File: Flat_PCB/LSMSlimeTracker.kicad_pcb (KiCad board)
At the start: 2 copper layers, 40 x 30.5 mm, 49 parts, among them J1 USB_C_Receptacle_USB2.0, J2 Conn_01x04_Socket, Q1 Q_PMOS_GSD, SW1 SW_Push, SW2 SW_SPDT, SW3 SW_Push, U1 LSM6DSV16X, U2 M3406, U3 ESP32-C3-WROOM-02-N4, U7 BQ24040DSQT

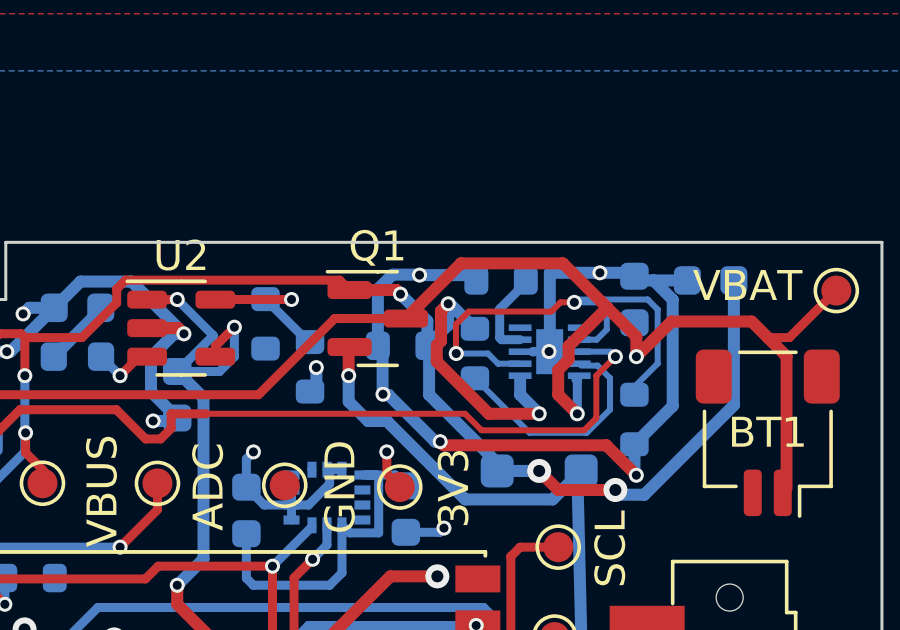
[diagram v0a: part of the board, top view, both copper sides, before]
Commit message: TTDM fix
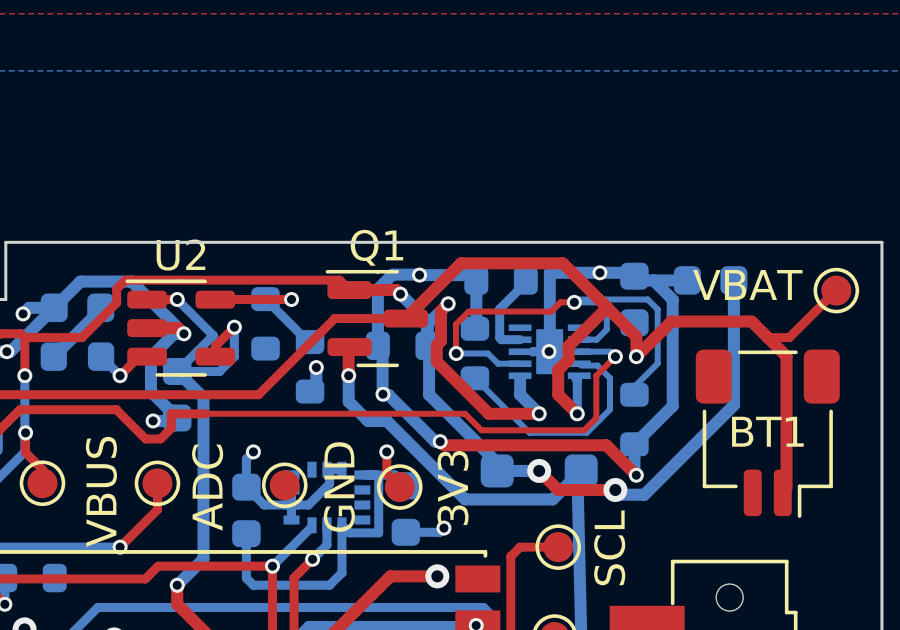
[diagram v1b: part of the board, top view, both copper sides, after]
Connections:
- R8 pad 2: +5V -> GND
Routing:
- net GND: track 72.7 -> 74.3 mm
- net +5V: track 61.3 -> 59.9 mm
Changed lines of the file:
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@@
       )
     )
-    (model "/Projects/kicad-custom-models/ESP32-C3-WROOM-02-N4.step"
+    (model "${KIPRJMOD}/custom-models/ESP32-C3-WROOM-02-N4.step"
       (offset (xyz 0 0 0))
       (scale (xyz 1 1 1))
@@
       (net 37 "/TS") (pintype "passive"))
     (pad "2" smd roundrect (at 0.825 0 90) (size 0.8 0.95) (layers "B.Cu" "B.Paste" "B.Mask") (roundrect_rratio 0.25)
-      (net 3 "+5V") (pintype "passive"))
+      (net 1 "GND") (pintype "passive"))
     (model "${KICAD6_3DMODEL_DIR}/Resistor_SMD.3dshapes/R_0603_1608Metric.wrl"
       (offset (xyz 0 0 0))
@@
     (pad "11" smd rect (at 0 0) (size 0.9 1.5) (layers "B.Cu" "B.Mask")
       (net 1 "GND") (pinfunction "EP") (pintype "bidirectional"))
-    (model "/Projects/kicad-custom-models/BQ24040DSQT.step"
+    (model "${KIPRJMOD}/custom-models/BQ24040DSQT.step"
       (offset (xyz 0 0 0))
       (scale (xyz 1 1 1))
@@
   (segment (start 182.88 54.567963) (end 183.291226 54.567963) (width 0.3) (layer "B.Cu") (net 1))
   (segment (start 171.572343 52.705) (end 171.572343 53.623467) (width 0.4) (layer "B.Cu") (net 1))
+  (segment (start 187.77 49.825077) (end 187.724238 49.870839) (width 0.4) (layer "B.Cu") (net 1))
   (segment (start 184.836117 52.07) (end 186.399927 53.63381) (width 0.4) (layer "B.Cu") (net 1))
   (segment (start 177.701164 52.943836) (end 177.8 52.845) (width 0.4) (layer "B.Cu") (net 1))
@@
   (segment (start 190.22 50.603401) (end 190.193419 50.629982) (width 0.4) (layer "B.Cu") (net 1))
   (segment (start 186.019256 65.477202) (end 186.055 65.512946) (width 0.4) (layer "B.Cu") (net 1))
+  (segment (start 187.77 48.26) (end 187.77 49.825077) (width 0.4) (layer "B.Cu") (net 1))
   (segment (start 182.88 55.041826) (end 182.88 54.567963) (width 0.3) (layer "B.Cu") (net 1))
   (segment (start 177.73975 70.19025) (end 177.8 70.13) (width 0.4) (layer "B.Cu") (net 1))
@@
   (segment (start 169.980041 49.809642) (end 168.187858 49.809642) (width 0.3) (layer "B.Cu") (net 3))
   (segment (start 189.865 52.705) (end 189.23 52.07) (width 0.4) (layer "B.Cu") (net 3))
+  (segment (start 186.138168 49.730364) (end 186.831766 49.036766) (width 0.4) (layer "B.Cu") (net 3))
   (segment (start 193.372025 55.403358) (end 192.563358 55.403358) (width 0.4) (layer "B.Cu") (net 3))
   (segment (start 172.72 53.975) (end 171.45 55.245) (width 0.3) (layer "B.Cu") (net 3))
@@
   (segment (start 188.465 54.61) (end 188.465 54.34) (width 0.4) (layer "B.Cu") (net 3))
   (segment (start 189.23 52.07) (end 189.23 51.535) (width 0.4) (layer "B.Cu") (net 3))
-  (segment (start 186.831766 49.036766) (end 186.831766 49.745647) (width 0.4) (layer "B.Cu") (net 3))
   (segment (start 186.195 52.07) (end 186.195 50.496077) (width 0.4) (layer "B.Cu") (net 3))
-  (segment (start 186.831766 49.745647) (end 186.013773 50.56364) (width 0.4) (layer "B.Cu") (net 3))
   (segment (start 186.138168 49.613167) (end 186.138168 50.439245) (width 0.4) (layer "B.Cu") (net 3))
   (segment (start 196.355 48.26) (end 196.355 52.420383) (width 0.4) (layer "B.Cu") (net 3))
+  (segment (start 186.138168 50.439245) (end 186.138168 49.730364) (width 0.4) (layer "B.Cu") (net 3))
   (segment (start 196.355 52.420383) (end 193.372025 55.403358) (width 0.4) (layer "B.Cu") (net 3))
   (segment (start 172.744541 53.341365) (end 172.72 53.365906) (width 0.3) (layer "B.Cu") (net 3))
@@
   (segment (start 185.242181 48.71718) (end 186.138168 49.613167) (width 0.4) (layer "B.Cu") (net 3))
   (segment (start 170.261049 50.09065) (end 169.980041 49.809642) (width 0.3) (layer "B.Cu") (net 3))
-  (segment (start 186.890165 49.036766) (end 187.724238 49.870839) (width 0.4) (layer "B.Cu") (net 3))
   (segment (start 170.343404 50.09065) (end 170.261049 50.09065) (width 0.3) (layer "B.Cu") (net 3))
   (segment (start 186.195 50.496077) (end 186.138168 50.439245) (width 0.4) (layer "B.Cu") (net 3))
@@
   (segment (start 168.857466 54.62) (end 167.9775 54.62) (width 0.3) (layer "B.Cu") (net 3))
   (segment (start 188.465 54.34) (end 186.195 52.07) (width 0.4) (layer "B.Cu") (net 3))
-  (segment (start 186.831766 49.036766) (end 186.890165 49.036766) (width 0.4) (layer "B.Cu") (net 3))
   (segment (start 162.56 49.53) (end 165.1 49.53) (width 0.3) (layer "F.Cu") (net 4))
   (segment (start 169.935717 53.636841) (end 169.893876 53.595) (width 0.3) (layer "B.Cu") (net 5))

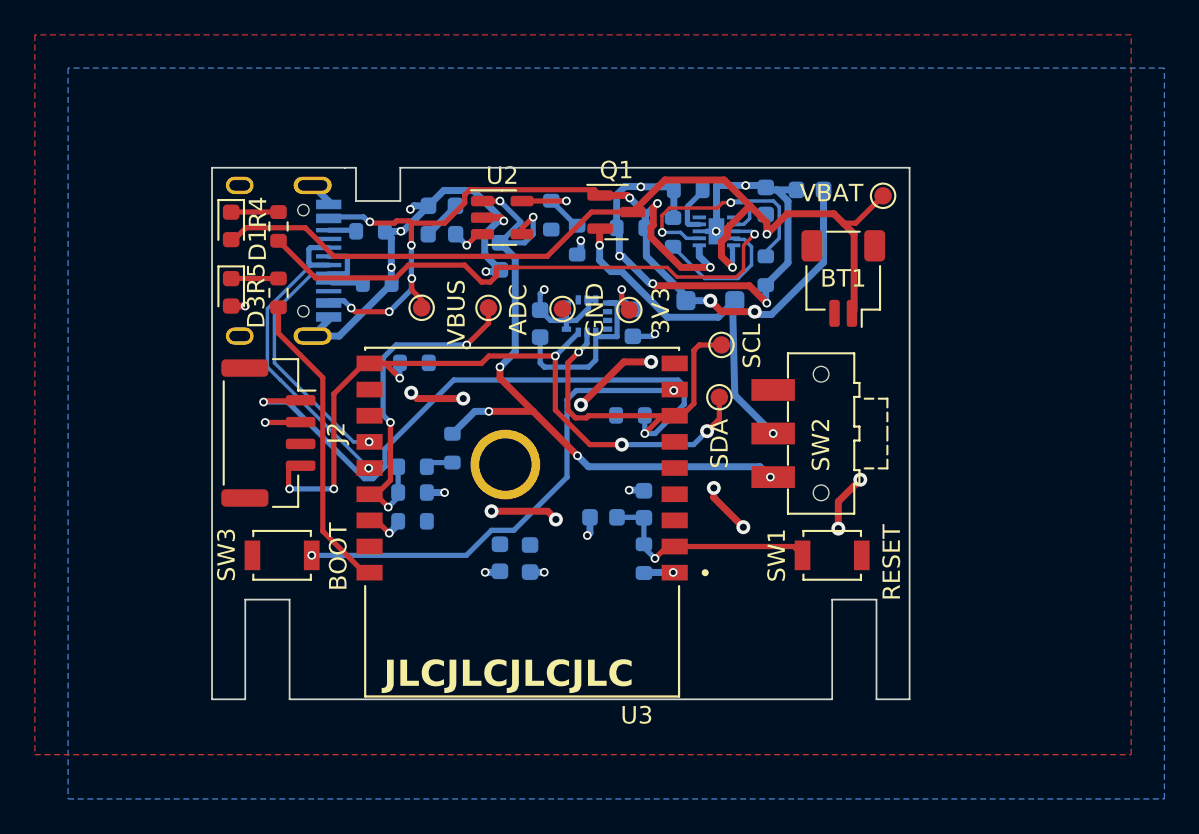
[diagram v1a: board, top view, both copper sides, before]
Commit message: Moved USB C to top
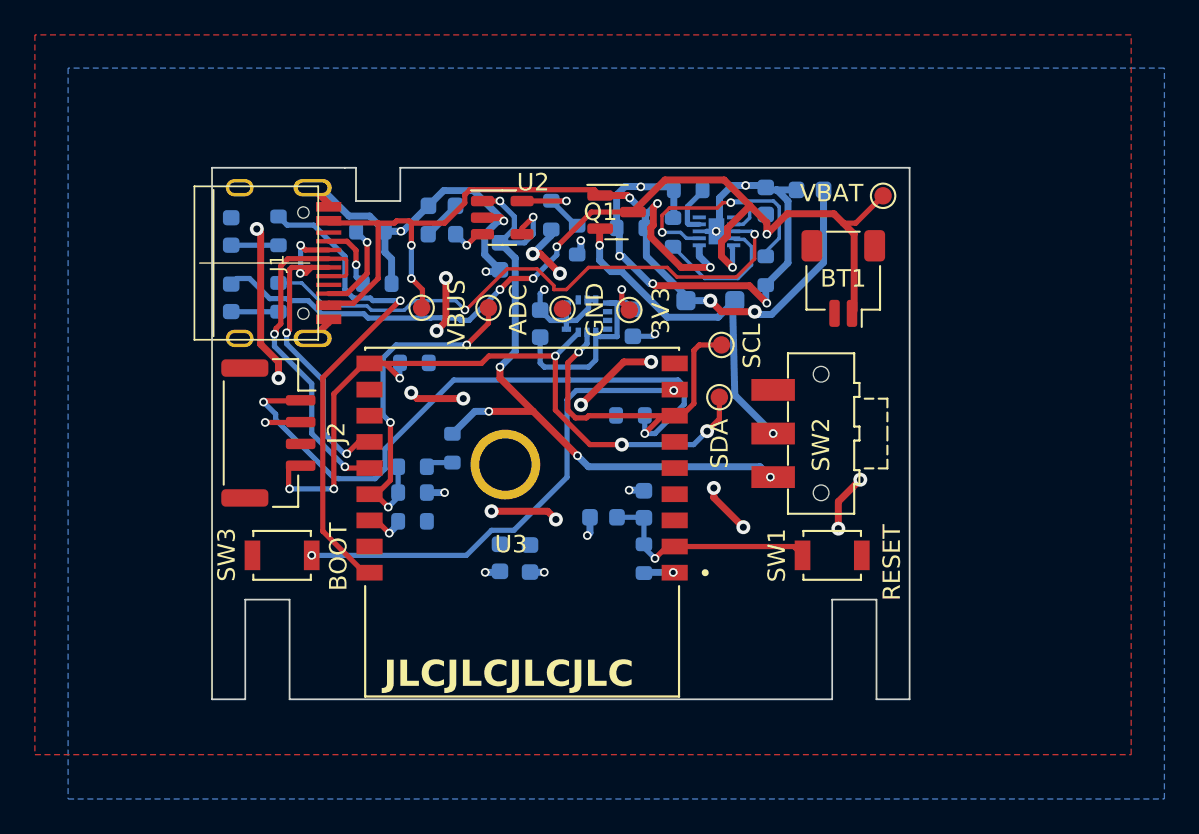
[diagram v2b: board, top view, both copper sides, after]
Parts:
- D1, D3, R4, R5: moved to B.Cu
- J1: moved to F.Cu
- moved D1 4.12 mm to (162.4, 54.4), turned to 90 degrees
- moved R4 4.07 mm to (165.1, 54.4), turned to -90 degrees
- moved R5 3.55 mm to (165.1, 50.6), turned to -90 degrees
- moved D3 3.49 mm to (162.4, 50.6), turned to 90 degrees
- moved J1 0.13 mm to (162.9, 52.5), turned to -90 degrees
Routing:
- net +3V3: track 37.5 -> 52.9 mm, vias 14 -> 19
- net /GPIO0: track 17.6 -> 28.8 mm, vias 0 -> 1
- net Net-(J1-CC2): track 1.60 -> 5.36 mm, vias 0 -> 1
- net /USBD-: track 17.4 -> 20.2 mm, vias 1 -> 4
- net GND: track 74.3 -> 72.1 mm, vias 19 -> 17
- net +BATT: track 55.1 -> 57.3 mm, vias 2 -> 5
- net Net-(J1-CC1): track 1.79 -> 3.86 mm, vias 0 -> 1
- net /USBD+: track 19.3 -> 20.7 mm, vias 1 -> 2
- net /CHRG: track 32.9 -> 33.9 mm, vias 1 -> 2
- net +5V: track 59.9 -> 60.4 mm, vias 10 -> 7

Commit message: V1.2
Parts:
- removed the C4 at (177.8, 52.1)
- removed the R1 at (172.8, 67.3)
- removed the R12 at (172.8, 65.6)
- removed the R13 at (175.1, 63.1)
- removed R20, R22: 5k1, Resistor_SMD:R_0603_1608Metric
- removed R21: 10k, Resistor_SMD:R_0603_1608Metric
- removed the R4 at (165.1, 54.4)
- added C6: 10uF, Capacitor_SMD:C_0603_1608Metric, B.Cu at (177.8, 52.1)
- added R10: 150k, Resistor_SMD:R_0603_1608Metric, B.Cu at (172.8, 65.8)
- added R14: 10k, Resistor_SMD:R_0603_1608Metric, B.Cu at (185.2, 61.2)
- added R15: 150k, Resistor_SMD:R_0603_1608Metric, B.Cu at (174.5, 63.5)
- added R16: 10k, Resistor_SMD:R_0603_1608Metric, B.Cu at (173.5, 58.3)
- added R17: 150k, Resistor_SMD:R_0603_1608Metric, B.Cu at (174.6, 62.0)
- added R18: 10k, Resistor_SMD:R_0603_1608Metric, B.Cu at (186.0, 69.5)
- added R6: 10k, Resistor_SMD:R_0603_1608Metric, B.Cu at (187.7, 50.8)
- added R9: 2k, Resistor_SMD:R_0603_1608Metric, B.Cu at (165.2, 50.6)
- R11: value 220k -> 150k
- R5: value 1k5 -> 150k
- R7: value 100k -> 2k
- R8: value 10k -> 5k1
- U1: footprint LGA_Custom:LGA14L_LSM6_STM -> LGA_Custom:Bosch_LGA-14_3x2.5mm_P0.5mm
- moved R8 23.0 mm to (172.8, 68.2), turned to 180 degrees
- moved R7 20.5 mm to (165.2, 54.5), turned to -90 degrees
- moved R5 20.3 mm to (185.4, 51.4), turned to 0 degrees
- moved R11 2.30 mm to (174.4, 65.8), turned to -90 degrees
- moved D1 1.27 mm to (189.9, 55.9)
- moved TP3 0.15 mm to (199.7, 48.7)
- moved U2 0.08 mm to (190.3, 50.6)
- renumbered C2 to C1, C1 to C2, C11 to C3, C12 to C4, C8 to C5, C9 to C7, C3 to C8, C5 to C9, D2 to D1, D1 to D2, J2 to J1, J1 to J2, R9 to R1, R3 to R12, R6 to R13, R10 to R2, R18 to R3, R19 to R4, SW2 to SW1, SW3 to SW2, SW1 to SW3, TP2 to TP1, TP1 to TP2, TP7 to TP3, TP5 to TP4, TP6 to TP5, TP3 to TP6, TP4 to TP7, U7 to U2, U2 to U4
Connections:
- D2 pad 1: Net-(D1-K) -> Net-(D2-K)
- R11 pad 1: Net-(R11-Pad1) -> /ADC
- R11 pad 2: /ADC -> GND
- R5 pad 1: /GPIO0 -> GND
- R5 pad 2: Net-(D3-K) -> +5V
- R7 pad 1: +5V -> /CHRG
- R7 pad 2: GND -> Net-(D2-K)
- R8 pad 1: /TS -> +3V3
- R8 pad 2: GND -> Net-(U3-IO2)
- U2 pad 9: /TS -> Net-(U2-TS)
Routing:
- net GND: track 72.1 -> 28.9 mm, vias 17 -> 16
- net +3V3: track 52.9 -> 23.4 mm, vias 19 -> 5
- net /SCL: track 54.7 -> 45.0 mm
- net /TS: track 7.76 -> 0.00 mm
- net Net-(U2-TS): track 0.00 -> 7.45 mm
- net +5V: track 60.4 -> 54.7 mm, vias 7 -> 3
- net VCC: track 39.9 -> 36.0 mm
- net Net-(U2-ISET): track 16.6 -> 13.1 mm
- net /USBD-: track 20.2 -> 17.4 mm
- net Net-(D2-K): track 0.00 -> 2.54 mm
- net Net-(D1-K): track 2.54 -> 0.00 mm
- net /SDA: track 42.9 -> 40.8 mm
- net +BATT: track 57.3 -> 55.1 mm, vias 5 -> 3
- net /CHRG: track 33.9 -> 32.0 mm
- net /GPIO0: track 28.8 -> 27.1 mm
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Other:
- outline, holes or cut-outs redrawn
- board text added: "+"
- board text added: "-"
- board text added: "."
- board text added: "v1.2 by Gorbit99"
- board text removed: "v1.0 by Gorbit99"
